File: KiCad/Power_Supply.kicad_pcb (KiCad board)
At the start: 4 copper layers, 59.7 x 65 mm, 60 parts, among them IC1 TPS63070RNMR, IC3 MCP1754ST-3302E_DB, J1 Jack-DC, J2 USB_B, J3 LCD_connector, J4 SWD, J5 TOP_OUT, U1 STM32F401RBTx, Y1 Crystal

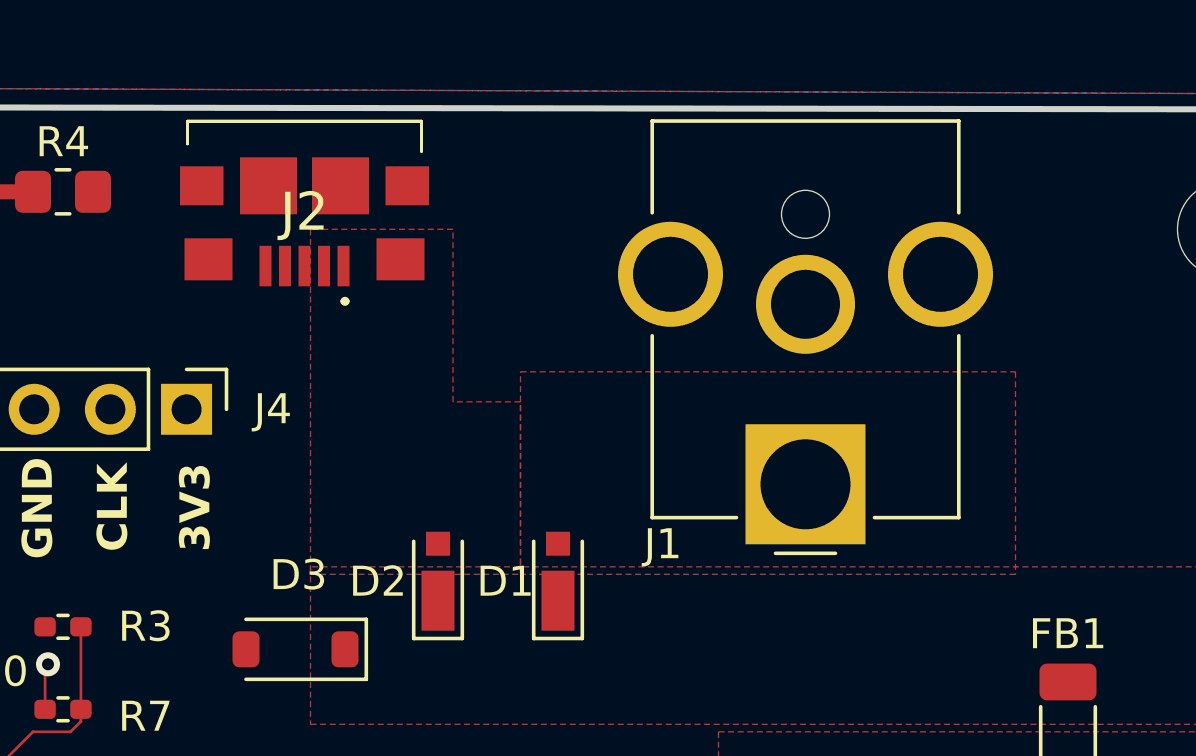
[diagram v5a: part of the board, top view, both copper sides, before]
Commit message: Removed unused LCD Docs
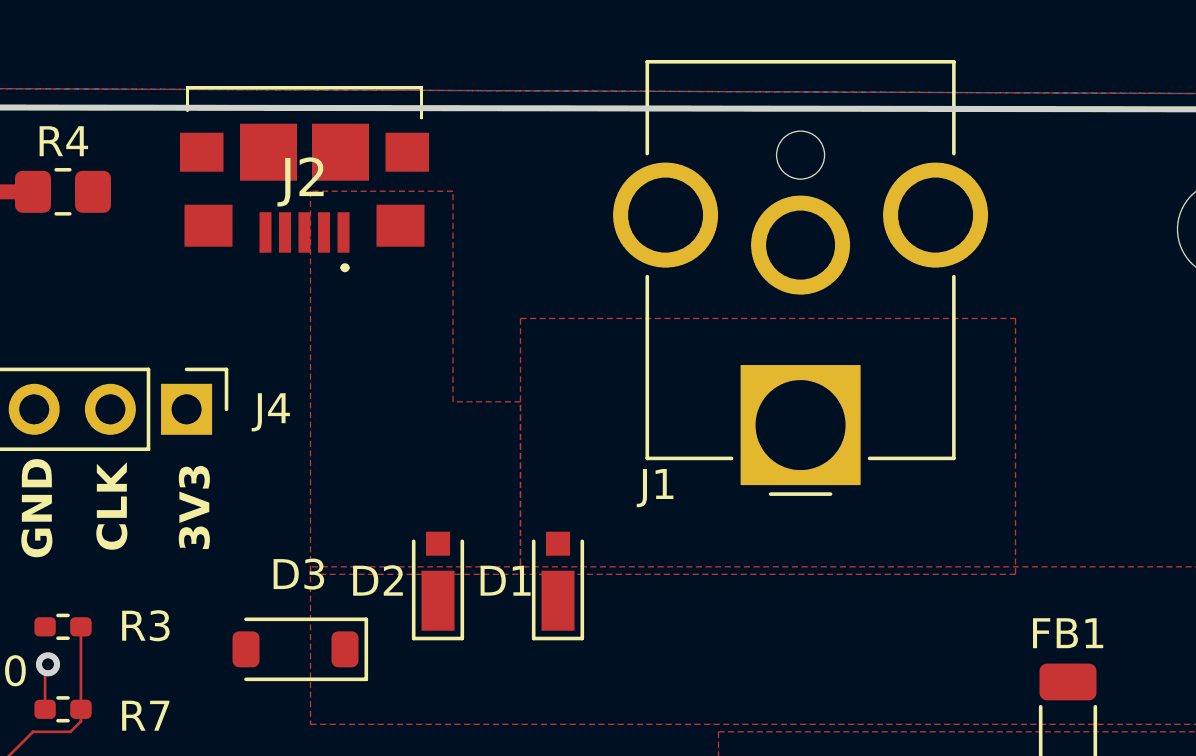
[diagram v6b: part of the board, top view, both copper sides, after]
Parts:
- moved J1 1.98 mm to (148.3, 58.3)
- moved J2 1.12 mm to (131.8, 49.5)
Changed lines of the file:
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@@
   )
   (footprint "Custom_eric:21745072" (layer "F.Cu")
-    (at 131.8 50.65 180)
+    (at 131.8 49.53 180)
     (descr "2174507-2-1")
     (tags "Connector")
@@
   )
   (footprint "Connector_BarrelJack:BarrelJack_CUI_PJ-063AH_Horizontal_CircularHoles" (layer "F.Cu")
-    (at 148.5 60.25 180)
+    (at 148.336 58.276 180)
     (descr "Barrel Jack, 2.0mm ID, 5.5mm OD, 24V, 8A, no switch, https://www.cui.com/product/resource/pj-063ah.pdf")
     (tags "barrel jack cui dc power")
@@
         (effects (font (size 1 1) (thickness 0.15)))
     )
-    (fp_text value "LCD_connector" (at 0 9.95) (layer "F.Fab")
+    (fp_text value "LCD_connector" (at -7.642 0.948) (layer "F.Fab")
         (effects (font (size 1 1) (thickness 0.15)))
     )
@@
     (polygon
       (pts
-        (xy 132 51.75)
+        (xy 132 50.48)
         (xy 132 63.25)
         (xy 139 63.25)
         (xy 139 57.5)
         (xy 136.75 57.5)
-        (xy 136.75 51.75)
+        (xy 136.75 50.48)
       )
     )
@@
     (polygon
       (pts
-        (xy 139 56.5)
-        (xy 155.5 56.5)
+        (xy 139 54.722)
+        (xy 155.5 54.722)
         (xy 155.5 63.25)
         (xy 139 63.25)
